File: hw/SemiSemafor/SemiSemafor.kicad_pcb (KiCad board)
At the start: 2 copper layers, 40.2 x 63.1 mm, 40 parts, among them J1 USB_PCB, J2 ESP-Programing_conector, SW1 SW_DIP_x01, SW2 SW_DIP_x01, U1 LD39200, U2 ESP32-C3-MINI-1

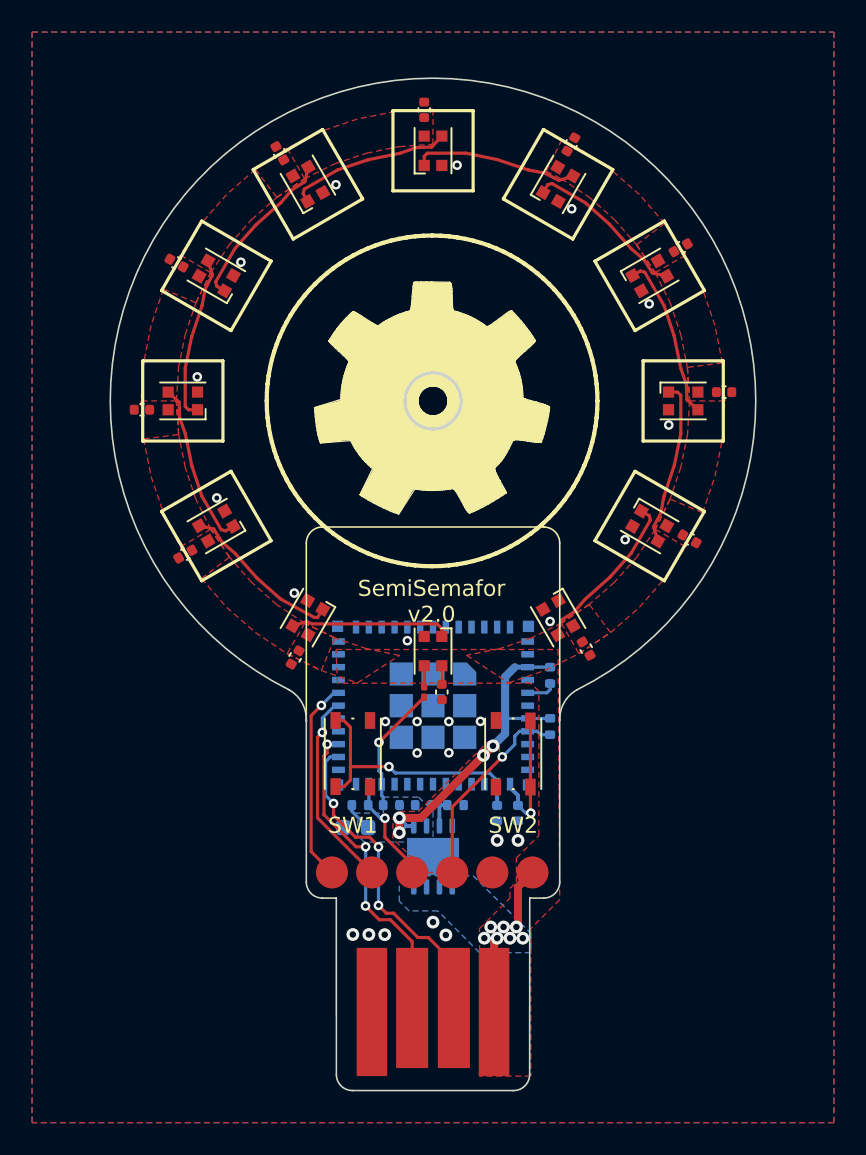
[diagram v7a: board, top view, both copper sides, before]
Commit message: 5mm LED
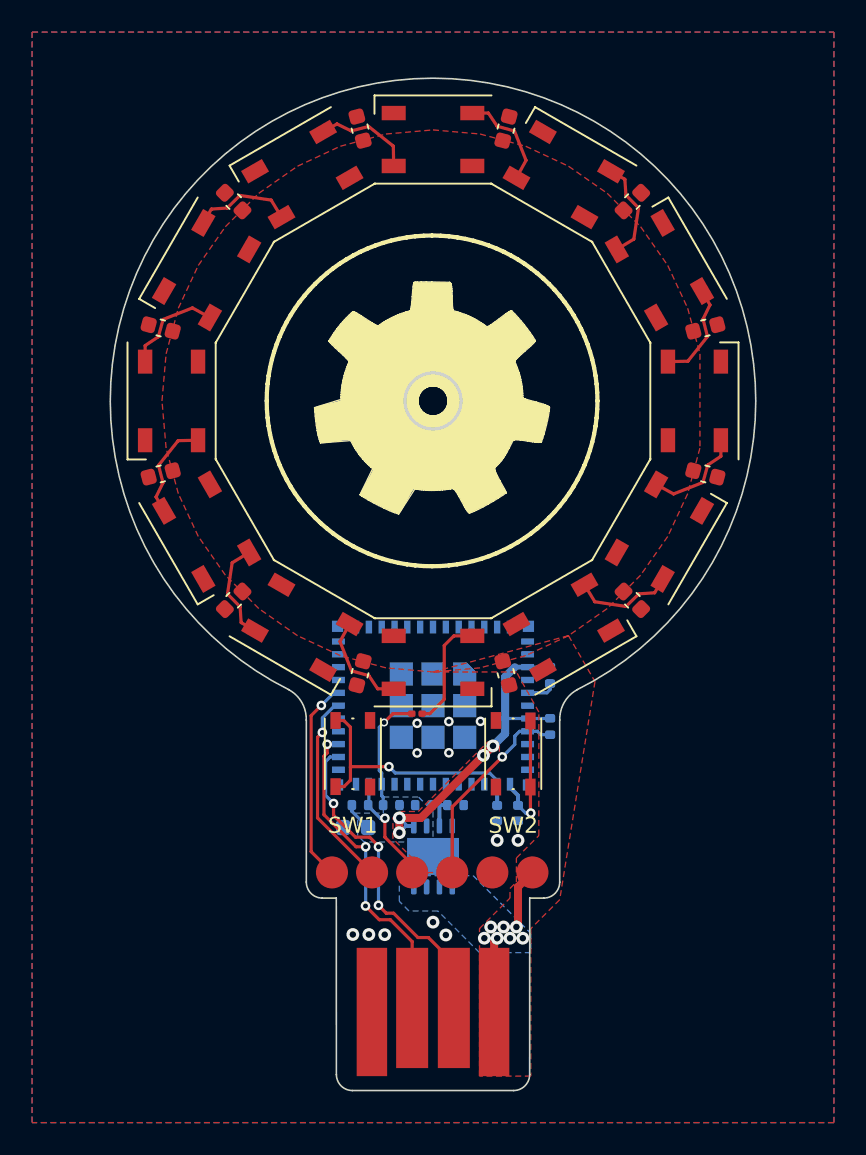
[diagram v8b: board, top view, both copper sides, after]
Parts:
- removed the D1 at (150.0, 95.6)
- added D7: WS2812B, LED_SMD:LED_WS2812B_PLCC4_5.0x5.0mm_P3.2mm, F.Cu at (150.0, 63.7)
- C1, C10, C11, C12, C13, C14, C15, C2, C3, C4, C5, C9: value 1u -> 100n; footprint Capacitor_SMD:C_0402_1005Metric -> Capacitor_SMD:C_0603_1608Metric
- D1: renamed from D7; footprint LED_SMD:LED_WS2812B-2020_PLCC4_2.0x2.0mm -> LED_SMD:LED_WS2812B_PLCC4_5.0x5.0mm_P3.2mm
- D10, D11, D12, D2, D3, D4, D5, D6, D8, D9: footprint LED_SMD:LED_WS2812B-2020_PLCC4_2.0x2.0mm -> LED_SMD:LED_WS2812B_PLCC4_5.0x5.0mm_P3.2mm
- moved D1 31.9 mm to (150.0, 96.3), turned to 0 degrees
- moved C11 5.23 mm to (162.4, 67.6), turned to 45 degrees
- moved C2 5.23 mm to (137.6, 92.4), turned to -135 degrees
- moved C14 5.23 mm to (162.4, 92.4), turned to -45 degrees
- moved C5 5.23 mm to (137.6, 67.6), turned to 135 degrees
- moved C12 5.23 mm to (167.0, 75.5), turned to 15 degrees
- moved C3 5.23 mm to (133.0, 84.5), turned to -165 degrees
- moved C9 5.23 mm to (145.5, 63.0), turned to 105 degrees
- moved C15 5.23 mm to (154.5, 97.0), turned to -75 degrees
- moved C1 5.23 mm to (145.4, 97.0), turned to -105 degrees
- moved C10 5.23 mm to (154.6, 63.0), turned to 75 degrees
- moved C13 5.23 mm to (167.0, 84.5), turned to -15 degrees
- moved C4 5.23 mm to (133.0, 75.5), turned to 165 degrees
- moved FB1 1.42 mm to (149.0, 99.5), turned to 0 degrees
- moved D11 0.70 mm to (164.1, 88.2), turned to 60 degrees
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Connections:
- D1 pad 1: Net-(D7-DOUT) -> +5V
- D1 pad 2: GND -> Net-(D1-DOUT)
- D1 pad 3: Net-(D6-DOUT) -> GND
- D1 pad 4: +5V -> Net-(D1-DIN)
- D10 pad 1: Net-(D10-DOUT) -> +5V
- D10 pad 2: GND -> Net-(D10-DOUT)
- D10 pad 3: Net-(D10-DIN) -> GND
- D10 pad 4: +5V -> Net-(D10-DIN)
- D11 pad 1: Net-(D11-DOUT) -> +5V
- D11 pad 2: GND -> Net-(D11-DOUT)
- D11 pad 3: Net-(D10-DOUT) -> GND
- D11 pad 4: +5V -> Net-(D10-DOUT)
- D12 pad 1: unconnected-(D12-DOUT-Pad1) -> +5V
- D12 pad 2: GND -> unconnected-(D12-DOUT-Pad2)
- D12 pad 3: Net-(D11-DOUT) -> GND
- D12 pad 4: +5V -> Net-(D11-DOUT)
- D2 pad 1: Net-(D2-DOUT) -> +5V
- D2 pad 2: GND -> Net-(D2-DOUT)
- D2 pad 3: Net-(D1-DOUT) -> GND
- D2 pad 4: +5V -> Net-(D1-DOUT)
- D3 pad 1: Net-(D3-DOUT) -> +5V
- D3 pad 2: GND -> Net-(D3-DOUT)
- D3 pad 3: Net-(D2-DOUT) -> GND
- D3 pad 4: +5V -> Net-(D2-DOUT)
- D4 pad 1: Net-(D4-DOUT) -> +5V
- D4 pad 2: GND -> Net-(D4-DOUT)
- D4 pad 3: Net-(D3-DOUT) -> GND
- D4 pad 4: +5V -> Net-(D3-DOUT)
- D5 pad 1: Net-(D5-DOUT) -> +5V
- D5 pad 2: GND -> Net-(D5-DOUT)
- D5 pad 3: Net-(D4-DOUT) -> GND
- D5 pad 4: +5V -> Net-(D4-DOUT)
- D6 pad 1: Net-(D6-DOUT) -> +5V
- D6 pad 2: GND -> Net-(D6-DOUT)
- D6 pad 3: Net-(D5-DOUT) -> GND
- D6 pad 4: +5V -> Net-(D5-DOUT)
- D8 pad 1: Net-(D8-DOUT) -> +5V
- D8 pad 2: GND -> Net-(D8-DOUT)
- D8 pad 3: Net-(D7-DOUT) -> GND
- D8 pad 4: +5V -> Net-(D7-DOUT)
- D9 pad 1: Net-(D10-DIN) -> +5V
- D9 pad 2: GND -> Net-(D10-DIN)
- D9 pad 3: Net-(D8-DOUT) -> GND
- D9 pad 4: +5V -> Net-(D8-DOUT)
- U2 pad 7: +3.3V -> (no net)
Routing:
- net Net-(D1-DIN): track 1.31 -> 7.10 mm
- net Net-(D6-DOUT): track 10.3 -> 6.32 mm
- net Net-(D3-DOUT): track 10.3 -> 6.32 mm
- net Net-(D10-DIN): track 10.3 -> 6.32 mm
- net Net-(D8-DOUT): track 10.3 -> 6.32 mm
- net Net-(D11-DOUT): track 10.3 -> 6.32 mm
- net Net-(D5-DOUT): track 10.3 -> 6.32 mm
- net Net-(D4-DOUT): track 10.3 -> 6.32 mm
- net Net-(D10-DOUT): track 10.3 -> 6.32 mm
- net Net-(D7-DOUT): track 10.3 -> 6.32 mm
- net Net-(D2-DOUT): track 10.2 -> 6.32 mm
- net Net-(D1-DOUT): track 9.96 -> 6.32 mm
- net +5V: track 9.65 -> 8.58 mm
- net /I-LED: track 8.01 -> 7.33 mm
- net GND: vias 25 -> 12
